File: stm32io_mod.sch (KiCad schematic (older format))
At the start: 44 parts, among them J1 UART, M1 BluePill, Q1 BC858, Q2 BC858, Q3 BC858, Q4 BC858, SW1 button_1, SW2 button_2, SW3 button_3, SW4 button_4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

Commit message: Se añade licencia
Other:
- note added: "MIT License\n\nCopyright (c) 2020 Matías S. Ávalos (msavalos@gmail.com)\n\nPermission is hereby granted, free of charge, to any person obtaining a copy\nof this software and associated documentation files (the "Software"), to deal\nin the Software without restriction, including without limitation the rights\nto use, copy, modify, merge, publish, distribute, sublicense, and/or sell\ncopies of the 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"
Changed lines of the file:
@@
 	1    0    0    -1
 $EndComp
+Text Notes 75   -50  0    106  ~ 0
+MIT License\n\nCopyright (c) 2020 Matías S. Ávalos (msavalos@gmail.com)\n\nPermission is hereby granted, free of charge, to any person obtaining a copy\nof this software and associated documentation files (the "Software"), to deal\nin the Software without restriction, including without limitation the rights\nto use, copy, modify, merge, publish, distribute, sublicense, and/or sell\ncopies of the Software, and to permit persons to whom the Software is\nfurnished to do so, subject to the following conditions:\n\nThe above copyright notice and this permission notice shall be included in all\ncopies or substantial portions of the Software.\n\nTHE SOFTWARE IS PROVIDED "AS IS", WITHOUT WARRANTY OF ANY KIND, EXPRESS OR\nIMPLIED, INCLUDING BUT NOT LIMITED TO THE WARRANTIES OF MERCHANTABILITY,\nFITNESS FOR A PARTICULAR PURPOSE AND NONINFRINGEMENT. IN NO EVENT SHALL THE\nAUTHORS OR COPYRIGHT HOLDERS BE LIABLE FOR ANY CLAIM, DAMAGES OR OTHER\nLIABILITY, WHETHER IN AN ACTION OF CONTRACT, TORT OR OTHERWISE, ARISING FROM,\nOUT OF OR IN CONNECTION WITH THE SOFTWARE OR THE USE OR OTHER DEALINGS IN THE\nSOFTWARE.\n
 $EndSCHEMATC

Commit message: cambio de resistencias a smd
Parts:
- R1, R11, R12, R13, R14, R16, R2: footprint Resistor_THT:R_Axial_DIN0204_L3.6mm_D1.6mm_P5.08mm_Horizontal -> Resistor_SMD:R_0805_2012Metric_Pad1.15x1.40mm_HandSolder
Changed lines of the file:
@@
 F 0 "R11" V 2800 5025 50  0000 C CNN
 F 1 "10k" V 2725 5025 50  0000 C CNN
-F 2 "Resistor_THT:R_Axial_DIN0204_L3.6mm_D1.6mm_P5.08mm_Horizontal" V 2730 5025 50  0001 C CNN
+F 2 "Resistor_SMD:R_0805_2012Metric_Pad1.15x1.40mm_HandSolder" V 2730 5025 50  0001 C CNN
 F 3 "~" H 2800 5025 50  0001 C CNN
 	1    2800 5025
@@
 F 0 "R1" V 1550 5025 50  0000 C CNN
 F 1 "10k" V 1475 5025 50  0000 C CNN
-F 2 "Resistor_THT:R_Axial_DIN0204_L3.6mm_D1.6mm_P5.08mm_Horizontal" V 1480 5025 50  0001 C CNN
+F 2 "Resistor_SMD:R_0805_2012Metric_Pad1.15x1.40mm_HandSolder" V 1480 5025 50  0001 C CNN
 F 3 "~" H 1550 5025 50  0001 C CNN
 	1    1550 5025
@@
 F 0 "R2" V 1550 5650 50  0000 C CNN
 F 1 "10k" V 1475 5650 50  0000 C CNN
-F 2 "Resistor_THT:R_Axial_DIN0204_L3.6mm_D1.6mm_P5.08mm_Horizontal" V 1480 5650 50  0001 C CNN
+F 2 "Resistor_SMD:R_0805_2012Metric_Pad1.15x1.40mm_HandSolder" V 1480 5650 50  0001 C CNN
 F 3 "~" H 1550 5650 50  0001 C CNN
 	1    1550 5650
@@
 F 0 "R16" V 4925 5300 50  0000 C CNN
 F 1 "10k" V 4850 5300 50  0000 C CNN
-F 2 "Resistor_THT:R_Axial_DIN0204_L3.6mm_D1.6mm_P5.08mm_Horizontal" V 4855 5300 50  0001 C CNN
+F 2 "Resistor_SMD:R_0805_2012Metric_Pad1.15x1.40mm_HandSolder" V 4855 5300 50  0001 C CNN
 F 3 "~" H 4925 5300 50  0001 C CNN
 	1    4925 5300
@@
 F 0 "R13" V 4075 5150 50  0000 C CNN
 F 1 "10k" V 4150 5150 50  0000 C CNN
-F 2 "Resistor_THT:R_Axial_DIN0204_L3.6mm_D1.6mm_P5.08mm_Horizontal" V 4005 5150 50  0001 C CNN
+F 2 "Resistor_SMD:R_0805_2012Metric_Pad1.15x1.40mm_HandSolder" V 4005 5150 50  0001 C CNN
 F 3 "~" H 4075 5150 50  0001 C CNN
 	1    4075 5150
@@
 F 0 "R14" V 4075 5650 50  0000 C CNN
 F 1 "10k" V 4150 5650 50  0000 C CNN
-F 2 "Resistor_THT:R_Axial_DIN0204_L3.6mm_D1.6mm_P5.08mm_Horizontal" V 4005 5650 50  0001 C CNN
+F 2 "Resistor_SMD:R_0805_2012Metric_Pad1.15x1.40mm_HandSolder" V 4005 5650 50  0001 C CNN
 F 3 "~" H 4075 5650 50  0001 C CNN
 	1    4075 5650
@@
 F 0 "R12" V 2800 5650 50  0000 C CNN
 F 1 "10k" V 2725 5650 50  0000 C CNN
-F 2 "Resistor_THT:R_Axial_DIN0204_L3.6mm_D1.6mm_P5.08mm_Horizontal" V 2730 5650 50  0001 C CNN
+F 2 "Resistor_SMD:R_0805_2012Metric_Pad1.15x1.40mm_HandSolder" V 2730 5650 50  0001 C CNN
 F 3 "~" H 2800 5650 50  0001 C CNN
 	1    2800 5650

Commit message: Pequeños arreglos en el PCB
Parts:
- D1: value LED_RGBC -> RGB
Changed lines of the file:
@@
 P 7500 5425
 F 0 "D1" H 7500 5922 50  0000 C CNN
-F 1 "LED_RGBC" H 7500 5831 50  0000 C CNN
+F 1 "RGB" H 7500 5831 50  0000 C CNN
 F 2 "LED_THT:LED_D5.0mm-4_RGB" H 7500 5375 50  0001 C CNN
 F 3 "~" H 7500 5375 50  0001 C CNN

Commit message: Agregado VCC al pinhead de la UART
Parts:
- J1: footprint Connector_PinHeader_2.54mm:PinHeader_1x03_P2.54mm_Vertical -> Connector_PinHeader_2.54mm:PinHeader_1x04_P2.54mm_Vertical; symbol Connector_Generic:Conn_01x03 -> Connector_Generic:Conn_01x04
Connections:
- net VCC: now also J1.4 (Pin_4)
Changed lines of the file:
@@
 P 4625 7150
 F 0 "#PWR0133" H 4625 6900 50  0001 C CNN
-F 1 "GND" H 4630 6977 50  0000 C CNN
+F 1 "GND" V 4625 6950 50  0000 C CNN
 F 2 "" H 4625 7150 50  0001 C CNN
 F 3 "" H 4625 7150 50  0001 C CNN
 	1    4625 7150
-	1    0    0    -1
+	0    -1   -1   0
 $EndComp
 Wire Notes Line width 12
@@
 $EndComp
 $Comp
-L Connector_Generic:Conn_01x03 J1
+L Connector_Generic:Conn_01x04 J1
 U 1 1 5E11F701
 P 4425 7050
 F 0 "J1" H 4425 7250 50  0000 C CNN
-F 1 "UART" H 4425 6850 50  0000 C CNN
-F 2 "Connector_PinHeader_2.54mm:PinHeader_1x03_P2.54mm_Vertical" H 4425 7050 50  0001 C CNN
+F 1 "UART" H 4425 6750 50  0000 C CNN
+F 2 "Connector_PinHeader_2.54mm:PinHeader_1x04_P2.54mm_Vertical" H 4425 7050 50  0001 C CNN
 F 3 "~" H 4425 7050 50  0001 C CNN
 	1    4425 7050
@@
 Text Notes 75   -50  0    106  ~ 0
 MIT License\n\nCopyright (c) 2020 Matías S. Ávalos (msavalos@gmail.com)\n\nPermission is hereby granted, free of charge, to any person obtaining a copy\nof this software and associated documentation files (the "Software"), to deal\nin the Software without restriction, including without limitation the rights\nto use, copy, modify, merge, publish, distribute, sublicense, and/or sell\ncopies of the Software, and to permit persons to whom the Software is\nfurnished to do so, subject to the following conditions:\n\nThe above copyright notice and this permission notice shall be included in all\ncopies or substantial portions of the Software.\n\nTHE SOFTWARE IS PROVIDED "AS IS", WITHOUT WARRANTY OF ANY KIND, EXPRESS OR\nIMPLIED, INCLUDING BUT NOT LIMITED TO THE WARRANTIES OF MERCHANTABILITY,\nFITNESS FOR A PARTICULAR PURPOSE AND NONINFRINGEMENT. IN NO EVENT SHALL THE\nAUTHORS OR COPYRIGHT HOLDERS BE LIABLE FOR ANY CLAIM, DAMAGES OR OTHER\nLIABILITY, WHETHER IN AN ACTION OF CONTRACT, TORT OR OTHERWISE, ARISING FROM,\nOUT OF OR IN CONNECTION WITH THE SOFTWARE OR THE USE OR OTHER DEALINGS IN THE\nSOFTWARE.\n
+$Comp
+L power:VCC #PWR0135
+U 1 1 5E67CE1D
+P 4625 7250
+F 0 "#PWR0135" H 4625 7100 50  0001 C CNN
+F 1 "VCC" V 4642 7378 50  0000 L CNN
+F 2 "" H 4625 7250 50  0001 C CNN
+F 3 "" H 4625 7250 50  0001 C CNN
+	1    4625 7250
+	0    1    1    0
+$EndComp
 $EndSCHEMATC

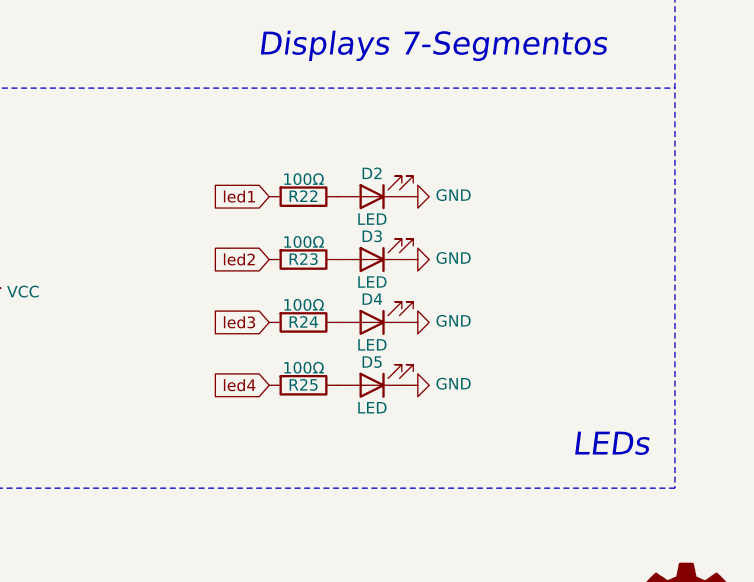
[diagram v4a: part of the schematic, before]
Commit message: Cambio de polaridad de los LEDs 2-5
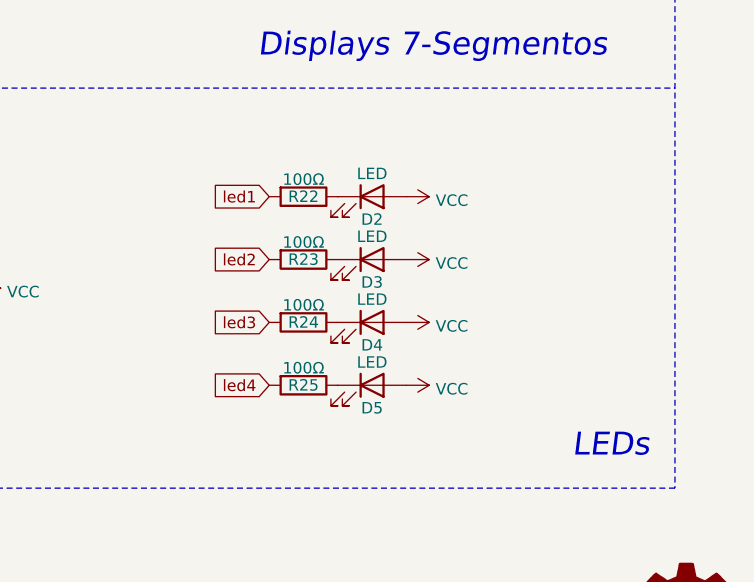
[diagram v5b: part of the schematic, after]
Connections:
- net GND: no longer D2.1 (K), D3.1 (K), D4.1 (K), D5.1 (K)
- net VCC: now also D2.2 (A), D3.2 (A), D4.2 (A), D5.2 (A)
- net at R22.1: now also D2.1 (K); no longer D2.2 (A)
- net at R23.1: now also D3.1 (K); no longer D3.2 (A)
- net at R24.1: now also D4.1 (K); no longer D4.2 (A)
- net at R25.1: now also D5.1 (K); no longer D5.2 (A)
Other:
- moved on the sheet: D2, D3, D4, D5
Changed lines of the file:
@@
 F 3 "~" H 9425 5025 50  0001 C CNN
 	1    9425 5025
-	-1   0    0    1
+	1    0    0    -1
 $EndComp
 $Comp
@@
 F 3 "~" H 9425 5300 50  0001 C CNN
 	1    9425 5300
-	-1   0    0    1
+	1    0    0    -1
 $EndComp
 $Comp
@@
 F 3 "~" H 9425 5575 50  0001 C CNN
 	1    9425 5575
-	-1   0    0    1
+	1    0    0    -1
 $EndComp
 $Comp
@@
 F 3 "~" H 9425 5850 50  0001 C CNN
 	1    9425 5850
-	-1   0    0    1
+	1    0    0    -1
 $EndComp
 $Comp
@@
 	1    9125 5850
 	0    1    1    0
-$EndComp
-$Comp
-L power:GND #PWR0123
-U 1 1 5E111EFE
-P 9575 5850
-F 0 "#PWR0123" H 9575 5600 50  0001 C CNN
-F 1 "GND" V 9580 5722 50  0000 R CNN
-F 2 "" H 9575 5850 50  0001 C CNN
-F 3 "" H 9575 5850 50  0001 C CNN
-	1    9575 5850
-	0    -1   -1   0
-$EndComp
-$Comp
-L power:GND #PWR0124
-U 1 1 5E1128AD
-P 9575 5575
-F 0 "#PWR0124" H 9575 5325 50  0001 C CNN
-F 1 "GND" V 9580 5447 50  0000 R CNN
-F 2 "" H 9575 5575 50  0001 C CNN
-F 3 "" H 9575 5575 50  0001 C CNN
-	1    9575 5575
-	0    -1   -1   0
-$EndComp
-$Comp
-L power:GND #PWR0125
-U 1 1 5E11366B
-P 9575 5300
-F 0 "#PWR0125" H 9575 5050 50  0001 C CNN
-F 1 "GND" V 9580 5172 50  0000 R CNN
-F 2 "" H 9575 5300 50  0001 C CNN
-F 3 "" H 9575 5300 50  0001 C CNN
-	1    9575 5300
-	0    -1   -1   0
-$EndComp
-$Comp
-L power:GND #PWR0126
-U 1 1 5E11382E
-P 9575 5025
-F 0 "#PWR0126" H 9575 4775 50  0001 C CNN
-F 1 "GND" V 9580 4897 50  0000 R CNN
-F 2 "" H 9575 5025 50  0001 C CNN
-F 3 "" H 9575 5025 50  0001 C CNN
-	1    9575 5025
-	0    -1   -1   0
 $EndComp
 $Comp
@@
 	0    1    1    0
 $EndComp
+$Comp
+L power:VCC #PWR0123
+U 1 1 5EC8D6F5
+P 9575 5025
+F 0 "#PWR0123" H 9575 4875 50  0001 C CNN
+F 1 "VCC" V 9592 5153 50  0000 L CNN
+F 2 "" H 9575 5025 50  0001 C CNN
+F 3 "" H 9575 5025 50  0001 C CNN
+	1    9575 5025
+	0    1    1    0
+$EndComp
+$Comp
+L power:VCC #PWR0124
+U 1 1 5EC8DB9F
+P 9575 5300
+F 0 "#PWR0124" H 9575 5150 50  0001 C CNN
+F 1 "VCC" V 9592 5428 50  0000 L CNN
+F 2 "" H 9575 5300 50  0001 C CNN
+F 3 "" H 9575 5300 50  0001 C CNN
+	1    9575 5300
+	0    1    1    0
+$EndComp
+$Comp
+L power:VCC #PWR0125
+U 1 1 5EC8E0DB
+P 9575 5575
+F 0 "#PWR0125" H 9575 5425 50  0001 C CNN
+F 1 "VCC" V 9592 5703 50  0000 L CNN
+F 2 "" H 9575 5575 50  0001 C CNN
+F 3 "" H 9575 5575 50  0001 C CNN
+	1    9575 5575
+	0    1    1    0
+$EndComp
+$Comp
+L power:VCC #PWR0126
+U 1 1 5EC8E53B
+P 9575 5850
+F 0 "#PWR0126" H 9575 5700 50  0001 C CNN
+F 1 "VCC" V 9592 5978 50  0000 L CNN
+F 2 "" H 9575 5850 50  0001 C CNN
+F 3 "" H 9575 5850 50  0001 C CNN
+	1    9575 5850
+	0    1    1    0
+$EndComp
